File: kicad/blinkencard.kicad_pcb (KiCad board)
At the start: 2 copper layers, 88.9 x 50.8 mm, 102 parts, among them J1 USB_B_Micro, Q1 BC847, Q2 BC847, Q3 BC847, Q4 BC847, Q5 BC847, SW1 0, SW2 1, SW3 LEFT, SW4 RIGHT, U1 ICE40UP5K-SG48ITR, U2 W25Q64JV, U3 CP2102N-A01-GQFN28, U4 MIC5504-1.2YM5, U5 MIC5504-3.3YM5

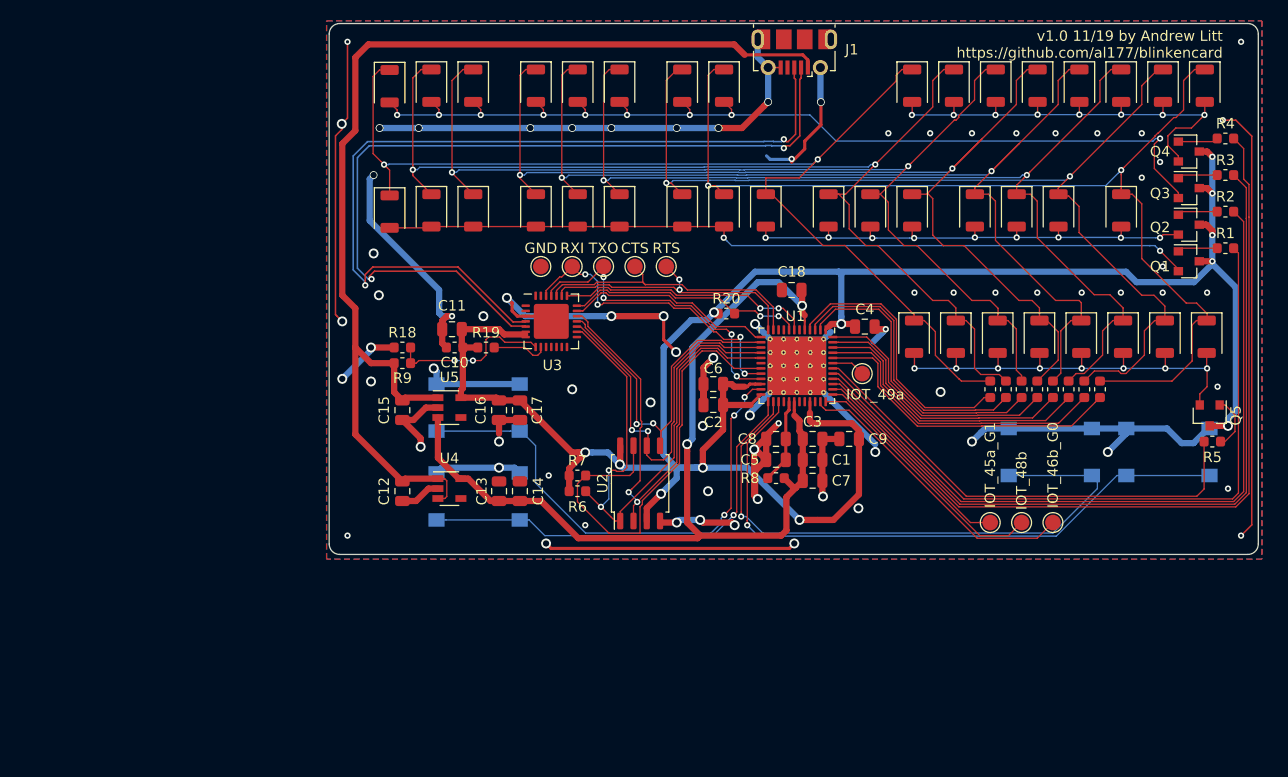
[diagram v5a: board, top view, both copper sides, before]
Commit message: Start v1.1 - minor fixes:
- Replace 4.7uF caps with 10uF
- Replace 0.01uF cap in the FPGA VCCPLL filter with 10uF per Lattice's design guideline
- All <1uF caps to 0603 sizes, 1-10uF to 0805
- Make TP? values match between schem and PCB
- Sanitize component values for BOM export consistency
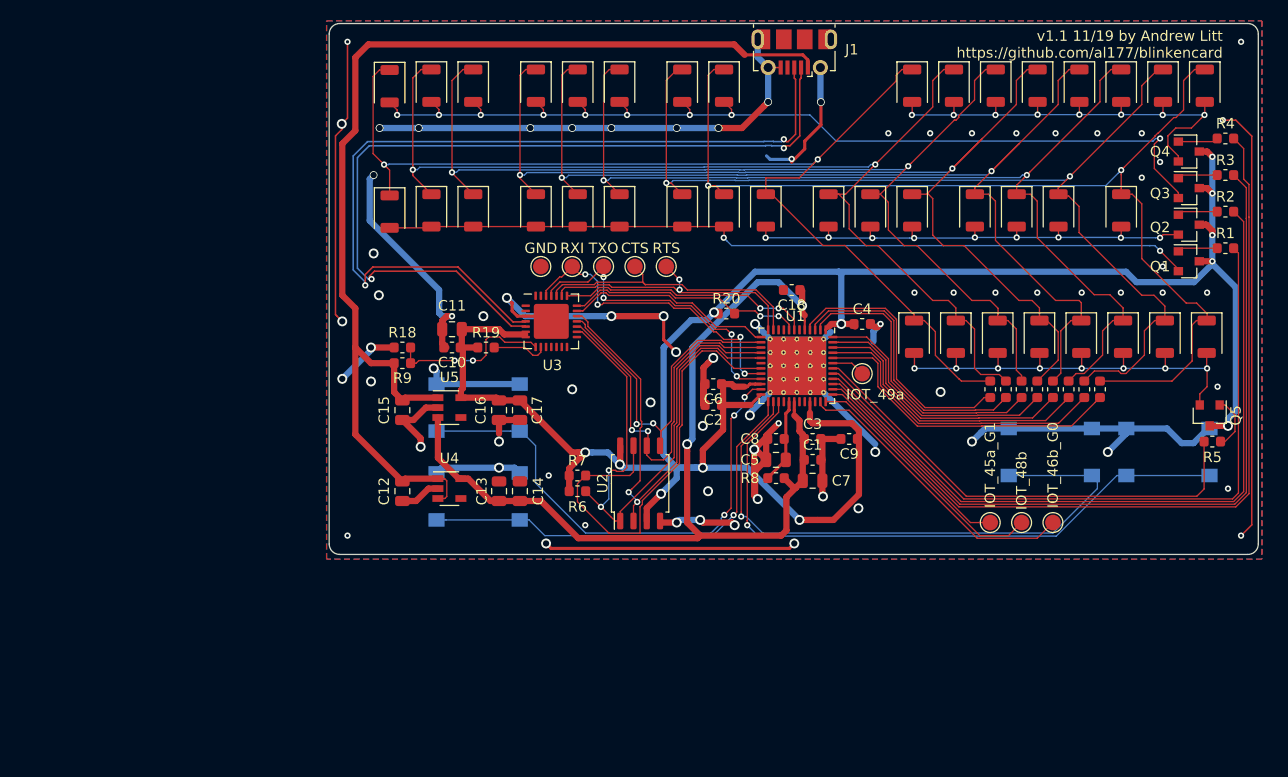
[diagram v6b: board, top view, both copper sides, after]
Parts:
- C1, C18, C2, C3, C4, C6, C8, C9: footprint Capacitor_SMD:C_0805_2012Metric -> Capacitor_SMD:C_0603_1608Metric
- C10: value .1uF -> 0.1uF
- C11: value 4.7uF -> 10.0uF
- C14, C17: value 10uF -> 10.0uF
- C5: value 0.01uF -> 10.0uF
- C7: value 1uF -> 1.0uF
- R1, R2, R3, R4, R5: value 1k -> 10k
- R10, R11, R12, R13, R14, R15, R16, R17: value 330 -> 270
- moved C4 0.35 mm to (51.0, 28.8)
- moved C10 0.25 mm to (11.8, 31.0)
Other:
- board text added: "v1.1 11/19 by Andrew Litt https://github.com/al177/blinkencard"
- board text removed: "v1.0 11/19 by Andrew Litt https://github.com/al177/blinkencard"

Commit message: Start v2.0 - change USB-UART to ESP32 and bugfixes
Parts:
- removed C16: 1.0uF, Capacitor_SMD:C_0805_2012Metric
- removed R18: 47.5K, Resistor_SMD:R_0603_1608Metric
- removed R19: 10k, Resistor_SMD:R_0603_1608Metric
- removed R7: 10K, Resistor_SMD:R_0603_1608Metric
- removed R9: 22.1K, Resistor_SMD:R_0603_1608Metric
- removed TP3: IOT_46b_G0, TestPoint:TestPoint_Pad_D1.5mm
- removed TP8: RXI, TestPoint:TestPoint_Pad_D1.5mm
- removed TP9: GND, TestPoint:TestPoint_Pad_D1.5mm
- removed U5: MIC5504-3.3YM5, Package_TO_SOT_SMD:SOT-23-5
- added J2: Conn_02x04_Odd_Even, Connector_PinHeader_2.54mm:PinHeader_2x04_P2.54mm_Vertical_SMD, F.Cu at (82.5, 44.2)
- C15: value 1.0uF -> 10.0uF
- R1, R2, R3, R4, R5: value 10k -> 10K
- TP1: value IOT_49a -> +5V
- TP2: value IOT_48b -> GND
- TP4: value IOT_45a_G1 -> IOT_42b
- TP5: value RTS -> IOT_43a
- TP6: value CTS -> IOT_44b
- TP7: value TXO -> GND
- U1: footprint Package_DFN_QFN:QFN-48-1EP_7x7mm_P0.5mm_EP5.6x5.6mm_ThermalVias -> Package_DFN_QFN:QFN-48-1EP_7x7mm_P0.5mm_EP5.15x5.15mm_ThermalVias
- U2: value W25Q64JV -> ESP32-WROOM-32; footprint Package_SO:SOIC-8_5.275x5.275mm_P1.27mm -> RF_Module:ESP32-WROOM-32
- U3: value CP2102N-A01-GQFN28 -> AP7361C-33E; footprint Package_DFN_QFN:QFN-28-1EP_5x5mm_P0.5mm_EP3.35x3.35mm -> Package_TO_SOT_SMD:SOT-223-3_TabPin2
- moved R6 54.6 mm to (-28.2, 28.2)
- moved TP6 47.5 mm to (41.7, 69.0)
- moved TP7 46.3 mm to (45.3, 65.5)
- moved TP5 43.3 mm to (41.7, 65.5)
- moved C12 41.6 mm to (44.2, 26.2)
- moved C17 40.7 mm to (-21.8, 29.2)
- moved U4 40.1 mm to (47.2, 26.2)
- moved C13 38.7 mm to (50.2, 26.2)
- moved C14 38.7 mm to (52.2, 26.2)
- moved TP4 32.9 mm to (38.2, 69.0)
- moved TP1 32.1 mm to (54.0, 65.5)
- moved C10 30.7 mm to (-17.5, 21.8)
- moved C11 22.8 mm to (-10.5, 24.2)
- moved C15 21.4 mm to (-13.5, 30.8)
- moved TP2 19.8 mm to (57.5, 65.5)
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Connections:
- C10 pad 1: VDD -> GND
- C10 pad 2: GND -> ESP_EN
- J1 pad 2: /usb_and_power/D- -> Net-(J1-Pad2)
- J1 pad 3: /usb_and_power/D+ -> Net-(J1-Pad3)
- R6 pad 2: FPGA_SS -> ESP_EN
- TP1 pad 1: Net-(TP1-Pad1) -> +5V
- TP2 pad 1: Net-(TP2-Pad1) -> GND
- TP5 pad 1: FPGA_RTS -> Net-(TP5-Pad1)
- TP6 pad 1: FPGA_CTS -> Net-(TP6-Pad1)
- TP7 pad 1: FPGA_TXO -> GND
- U1 pad 11: FPGA_CTS -> Net-(U1-Pad11)
- U1 pad 12: FPGA_RTS -> Net-(U1-Pad12)
- U1 pad 14: FPGA_SO_FLASH_MOSI -> FPGA_SO
- U1 pad 17: FPGA_SI_FLASH_MISO -> FPGA_SI
- U1 pad 19: FLASH_HOLDn -> Net-(U1-Pad19)
- U1 pad 28: Net-(U1-Pad28) -> Net-(TP6-Pad1)
- U1 pad 31: Net-(U1-Pad31) -> Net-(TP5-Pad1)
- U1 pad 32: Net-(U1-Pad32) -> Net-(TP4-Pad1)
- U1 pad 34: Net-(U1-Pad34) -> LED_ROW_3
- U1 pad 35: Net-(TP3-Pad1) -> LED_ROW_2
- U1 pad 36: Net-(TP2-Pad1) -> LED_ROW_1
- U1 pad 37: Net-(TP4-Pad1) -> LED_ROW_0
- U1 pad 38: LED_ROW_3 -> LED_ROW_4
- U1 pad 39: LED_ROW_2 -> Net-(U1-Pad39)
- U1 pad 40: LED_ROW_1 -> Net-(U1-Pad40)
- U1 pad 41: LED_ROW_0 -> Net-(U1-Pad41)
- U1 pad 42: LED_ROW_4 -> Net-(U1-Pad42)
- U1 pad 43: Net-(TP1-Pad1) -> Net-(U1-Pad43)
- U2 pad 1: FPGA_SS -> GND
- U2 pad 2: FPGA_SI_FLASH_MISO -> VDD
- U2 pad 3: VDD -> ESP_EN
- U2 pad 4: GND -> Net-(U2-Pad4)
- U2 pad 5: FPGA_SO_FLASH_MOSI -> Net-(U2-Pad5)
- U2 pad 6: FPGA_SCK -> Net-(U2-Pad6)
- U2 pad 7: FLASH_HOLDn -> Net-(U2-Pad7)
- U2 pad 8: VDD -> Net-(U2-Pad8)
- U3 pad 1: Net-(U3-Pad1) -> +5V
- U3 pad 2: Net-(U3-Pad2) -> GND
- U3 pad 3: GND -> VDD
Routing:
- net GND: track 337.5 -> 114.2 mm, vias 77 -> 39
- net ESP_BOOTLOADER: track 0.00 -> 124.2 mm, vias 0 -> 2
- net ESP_RXD0: track 0.00 -> 108.9 mm, vias 0 -> 2
- net ESP_TXD0: track 0.00 -> 101.8 mm, vias 0 -> 2
- net VDD: track 216.4 -> 131.5 mm, vias 12 -> 10
- net /usb_and_power/D+: track 81.6 -> 0.00 mm, vias 2 -> 0
- net /usb_and_power/D-: track 80.0 -> 0.00 mm, vias 2 -> 0
- net ESP_EN: track 0.00 -> 76.2 mm
- net +5V: track 107.2 -> 39.1 mm
- net BUTTON_L: track 60.1 -> 0.00 mm, vias 1 -> 0
- net BUTTON_R: track 57.7 -> 0.00 mm, vias 1 -> 0
- net BUTTON_1: track 48.6 -> 0.00 mm, vias 3 -> 0
- net FPGA_SI_FLASH_MISO: track 46.8 -> 0.00 mm, vias 2 -> 0
- net FLASH_HOLDn: track 43.9 -> 0.00 mm
- net BUTTON_0: track 42.2 -> 0.00 mm, vias 1 -> 0
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
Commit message: Finish routing v2.0.
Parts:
- moved R6 113.2 mm to (84.8, 35.2), turned to 270 degrees
- moved C10 104.6 mm to (86.2, 35.2), turned to 270 degrees
- moved TP2 58.6 mm to (34.2, 11.8)
- moved TP1 55.0 mm to (42.5, 11.8)
- moved C15 49.6 mm to (35.5, 23.2)
- moved C17 47.6 mm to (25.5, 23.2)
- moved C11 43.3 mm to (28.2, 43.5), turned to 90 degrees
- moved TP6 33.4 mm to (63.0, 43.2)
- moved TP4 32.2 mm to (57.5, 43.2)
- moved TP7 30.2 mm to (65.8, 43.2)
- moved TP5 28.9 mm to (60.2, 43.2)
- moved R5 3.55 mm to (79.8, 35.2), turned to 270 degrees
- moved SW2 2.75 mm to (14.2, 34.0)
- turned J2 to 90 degrees
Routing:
- net GND: track 114.2 -> 242.5 mm, vias 39 -> 89
- net VDD: track 131.5 -> 190.9 mm, vias 10 -> 18
- net BUTTON_1: track 0.00 -> 50.3 mm, vias 0 -> 1
- net BUTTON_L: track 0.00 -> 46.7 mm, vias 0 -> 1
- net BUTTON_0: track 0.00 -> 41.0 mm, vias 0 -> 1
- net BUTTON_R: track 0.00 -> 34.0 mm, vias 0 -> 1
- net FPGA_CRESET: track 6.38 -> 39.2 mm
- net Net-(TP6-Pad1): track 0.00 -> 22.6 mm, vias 0 -> 2
- net Net-(TP5-Pad1): track 0.00 -> 18.2 mm, vias 0 -> 2
- net Net-(TP4-Pad1): track 0.00 -> 15.1 mm, vias 0 -> 2
- net ESP_EN: track 76.2 -> 90.5 mm, vias 0 -> 2
- net ESP_BOOTLOADER: track 124.2 -> 113.6 mm
- net ESP_TXD0: track 101.8 -> 94.4 mm
- net ESP_RXD0: track 108.9 -> 102.6 mm
- net Net-(D50-Pad2): track 40.0 -> 44.6 mm
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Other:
- net class PWR: via_dia 0.95 -> 0.6; via_drill 0.6 -> 0.3
- board text added: "v2.0 12/19 by Andrew Litt https://github.com/al177/blinkencard"
- board text removed: "v1.1 11/19 by Andrew Litt https://github.com/al177/blinkencard"
